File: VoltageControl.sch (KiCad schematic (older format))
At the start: 7 parts

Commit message: Annotation completed
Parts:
- gave numbers to parts that had none: 7
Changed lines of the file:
@@
 $EndDescr
 $Comp
-L LMV358 U?
+L LMV358 U201
 U 2 1 57DB8C8A
 P 3700 4100
-F 0 "U?" H 3650 4300 50  0000 L CNN
+F 0 "U201" H 3650 4300 50  0000 L CNN
 F 1 "LMV358" H 3650 3850 50  0000 L CNN
 F 2 "" H 3700 4100 50  0000 C CNN
@@
 $EndComp
 $Comp
-L R R?
+L R R301
 U 1 1 57DB8C91
 P 2600 5200
-F 0 "R?" V 2680 5200 50  0000 C CNN
+F 0 "R301" V 2680 5200 50  0000 C CNN
 F 1 "R" V 2600 5200 50  0000 C CNN
 F 2 "" V 2530 5200 50  0000 C CNN
@@
 $EndComp
 $Comp
-L GND #PWR?
+L GND #PWR302
 U 1 1 57DB8C98
 P 3600 4400
-F 0 "#PWR?" H 3600 4150 50  0001 C CNN
+F 0 "#PWR302" H 3600 4150 50  0001 C CNN
 F 1 "GND" H 3600 4250 50  0000 C CNN
 F 2 "" H 3600 4400 50  0000 C CNN
@@
 $EndComp
 $Comp
-L POT RV?
+L POT RV301
 U 1 1 57DB8C9E
 P 2600 4450
-F 0 "RV?" H 2600 4370 50  0000 C CNN
+F 0 "RV301" H 2600 4370 50  0000 C CNN
 F 1 "POT" H 2600 4450 50  0000 C CNN
 F 2 "" H 2600 4450 50  0000 C CNN
@@
 $EndComp
 $Comp
-L C C?
+L C C301
 U 1 1 57DB8CA5
 P 3200 3450
-F 0 "C?" H 3225 3550 50  0000 L CNN
+F 0 "C301" H 3225 3550 50  0000 L CNN
 F 1 "C" H 3225 3350 50  0000 L CNN
 F 2 "" H 3238 3300 50  0000 C CNN
@@
 $EndComp
 $Comp
-L GND #PWR?
+L GND #PWR301
 U 1 1 57DB8CAC
 P 3200 3600
-F 0 "#PWR?" H 3200 3350 50  0001 C CNN
+F 0 "#PWR301" H 3200 3350 50  0001 C CNN
 F 1 "GND" H 3200 3450 50  0000 C CNN
 F 2 "" H 3200 3600 50  0000 C CNN
@@
 	1850 2250 2750 2250
 $Comp
-L D D?
+L D D301
 U 1 1 57DB8D2E
 P 4350 4100
-F 0 "D?" H 4350 4200 50  0000 C CNN
+F 0 "D301" H 4350 4200 50  0000 C CNN
 F 1 "D" H 4350 4000 50  0000 C CNN
 F 2 "" H 4350 4100 50  0000 C CNN
@@
 $EndComp
 $Comp
-L R R?
+L R R303
 U 1 1 57DB8DD7
 P 5400 4950
-F 0 "R?" V 5480 4950 50  0000 C CNN
+F 0 "R303" V 5480 4950 50  0000 C CNN
 F 1 "1k" V 5400 4950 50  0000 C CNN
 F 2 "" V 5330 4950 50  0000 C CNN
@@
 $EndComp
 $Comp
-L R R?
+L R R302
 U 1 1 57DB8E45
 P 5400 4400
-F 0 "R?" V 5480 4400 50  0000 C CNN
+F 0 "R302" V 5480 4400 50  0000 C CNN
 F 1 "9k" V 5400 4400 50  0000 C CNN
 F 2 "" V 5330 4400 50  0000 C CNN

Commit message: Add initial layout
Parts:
- C301: footprint (none) -> Capacitors_SMD:C_0805
- D301: footprint (none) -> Diodes_SMD:SMB-SMC_Universal_Handsoldering; MPN (none) -> 1N914BWT
- R301, R302, R303: footprint (none) -> Resistors_SMD:R_0805
- RV301: footprint (none) -> Potentiometers:Potentiometer_WirePads_largePads
- U301: renamed from U201; footprint (none) -> SMD_Packages:SOIC-8-N
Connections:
- net at R301.1, RV301.3: now also U301.3 (+); no longer U301.5 (+)
- net at R302.2, R303.1: now also U301.2 (-); no longer U301.6 (-)
- net at D301.1 (K): now also U301.1; no longer U301.7
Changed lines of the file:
@@
 $EndDescr
 $Comp
-L LMV358 U201
-U 2 1 57DB8C8A
+L LMV358 U301
+U 1 1 57DB8C8A
 P 3700 4100
-F 0 "U201" H 3650 4300 50  0000 L CNN
+F 0 "U301" H 3650 4300 50  0000 L CNN
 F 1 "LMV358" H 3650 3850 50  0000 L CNN
-F 2 "" H 3700 4100 50  0000 C CNN
+F 2 "SMD_Packages:SOIC-8-N" H 3700 4100 50  0001 C CNN
 F 3 "" H 3700 4100 50  0000 C CNN
-	2    3700 4100
+	1    3700 4100
 	1    0    0    -1
 $EndComp
@@
 F 0 "R301" V 2680 5200 50  0000 C CNN
 F 1 "R" V 2600 5200 50  0000 C CNN
-F 2 "" V 2530 5200 50  0000 C CNN
+F 2 "Resistors_SMD:R_0805" V 2530 5200 50  0001 C CNN
 F 3 "" H 2600 5200 50  0000 C CNN
 	1    2600 5200
@@
 $EndComp
 $Comp
-L GND #PWR302
+L GND #PWR05
 U 1 1 57DB8C98
 P 3600 4400
-F 0 "#PWR302" H 3600 4150 50  0001 C CNN
+F 0 "#PWR05" H 3600 4150 50  0001 C CNN
 F 1 "GND" H 3600 4250 50  0000 C CNN
 F 2 "" H 3600 4400 50  0000 C CNN
@@
 F 0 "RV301" H 2600 4370 50  0000 C CNN
 F 1 "POT" H 2600 4450 50  0000 C CNN
-F 2 "" H 2600 4450 50  0000 C CNN
+F 2 "Potentiometers:Potentiometer_WirePads_largePads" H 2600 4450 50  0001 C CNN
 F 3 "" H 2600 4450 50  0000 C CNN
 	1    2600 4450
@@
 F 0 "C301" H 3225 3550 50  0000 L CNN
 F 1 "C" H 3225 3350 50  0000 L CNN
-F 2 "" H 3238 3300 50  0000 C CNN
+F 2 "Capacitors_SMD:C_0805" H 3238 3300 50  0001 C CNN
 F 3 "" H 3200 3450 50  0000 C CNN
 	1    3200 3450
@@
 $EndComp
 $Comp
-L GND #PWR301
+L GND #PWR06
 U 1 1 57DB8CAC
 P 3200 3600
-F 0 "#PWR301" H 3200 3350 50  0001 C CNN
+F 0 "#PWR06" H 3200 3350 50  0001 C CNN
 F 1 "GND" H 3200 3450 50  0000 C CNN
 F 2 "" H 3200 3600 50  0000 C CNN
@@
 F 0 "D301" H 4350 4200 50  0000 C CNN
 F 1 "D" H 4350 4000 50  0000 C CNN
-F 2 "" H 4350 4100 50  0000 C CNN
-F 3 "" H 4350 4100 50  0000 C CNN
+F 2 "Diodes_SMD:SMB-SMC_Universal_Handsoldering" H 4350 4100 50  0001 C CNN
+F 3 "http://www.fairchildsemi.com/datasheets/1N/1N914BWT.pdf" H 4350 4100 50  0001 C CNN
+F 4 "1N914BWT" H 4350 4100 60  0001 C CNN "MPN"
 	1    4350 4100
 	1    0    0    -1
@@
 F 0 "R303" V 5480 4950 50  0000 C CNN
 F 1 "1k" V 5400 4950 50  0000 C CNN
-F 2 "" V 5330 4950 50  0000 C CNN
+F 2 "Resistors_SMD:R_0805" V 5330 4950 50  0001 C CNN
 F 3 "" H 5400 4950 50  0000 C CNN
 	1    5400 4950
@@
 F 0 "R302" V 5480 4400 50  0000 C CNN
 F 1 "9k" V 5400 4400 50  0000 C CNN
-F 2 "" V 5330 4400 50  0000 C CNN
+F 2 "Resistors_SMD:R_0805" V 5330 4400 50  0001 C CNN
 F 3 "" H 5400 4400 50  0000 C CNN
 	1    5400 4400

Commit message: Add heat sink footprint
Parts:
- D301: MPN 1N914BWT -> CD214B-R3600
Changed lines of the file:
@@
 F 1 "D" H 4350 4000 50  0000 C CNN
 F 2 "Diodes_SMD:SMB-SMC_Universal_Handsoldering" H 4350 4100 50  0001 C CNN
-F 3 "http://www.fairchildsemi.com/datasheets/1N/1N914BWT.pdf" H 4350 4100 50  0001 C CNN
-F 4 "1N914BWT" H 4350 4100 60  0001 C CNN "MPN"
+F 3 "http://www.bourns.com/docs/Product-Datasheets/CD214B-R350_R31000.pdf" H 4350 4100 50  0001 C CNN
+F 4 "CD214B-R3600" H 4350 4100 60  0001 C CNN "MPN"
 	1    4350 4100
 	1    0    0    -1

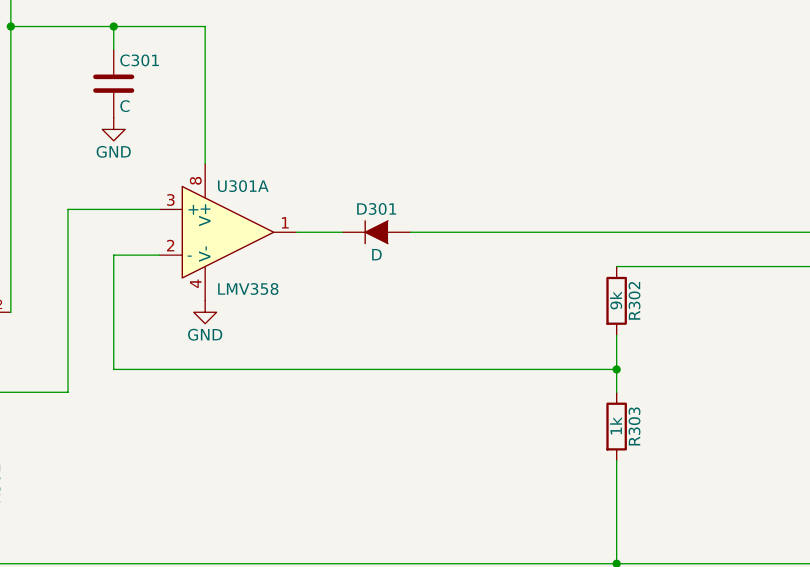
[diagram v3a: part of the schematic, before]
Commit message: Remove extra erroneus LMV358
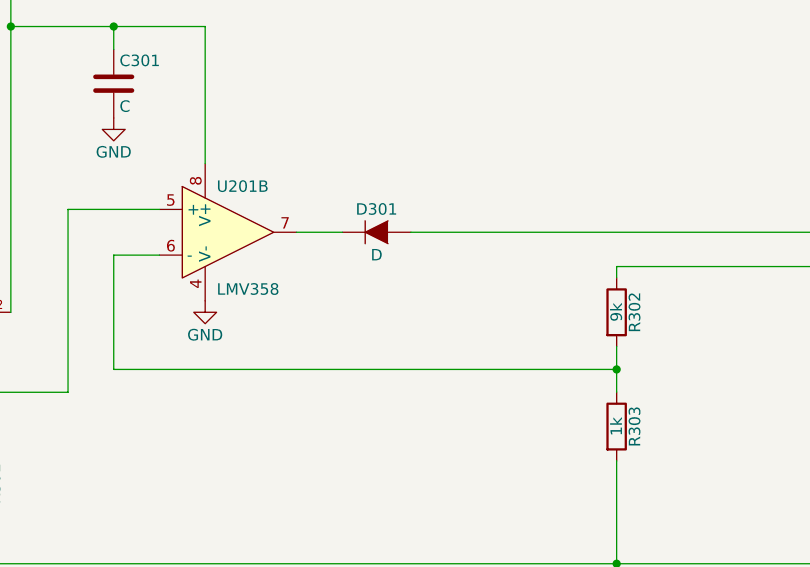
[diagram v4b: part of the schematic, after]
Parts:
- removed U301: LMV358, SMD_Packages:SOIC-8-N, symbol LMV358
- added U201: LMV358, SMD_Packages:SOIC-8-N, symbol LMV358
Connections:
- net 2.7V: now also U201.8 (V+)
- net GND: now also U201.4 (V-)
- net at D301.1 (K): now also U201.7
- net at R302.2, R303.1: now also U201.6 (-)
- net at R301.1, RV301.3: now also U201.5 (+)
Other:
- moved on the sheet: R302
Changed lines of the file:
@@
 $EndDescr
-$Comp
-L LMV358 U301
-U 1 1 57DB8C8A
-P 3700 4100
-F 0 "U301" H 3650 4300 50  0000 L CNN
-F 1 "LMV358" H 3650 3850 50  0000 L CNN
-F 2 "SMD_Packages:SOIC-8-N" H 3700 4100 50  0001 C CNN
-F 3 "" H 3700 4100 50  0000 C CNN
-	1    3700 4100
-	1    0    0    -1
-$EndComp
 $Comp
 L R R301
@@
 L R R302
 U 1 1 57DB8E45
-P 5400 4400
-F 0 "R302" V 5480 4400 50  0000 C CNN
-F 1 "9k" V 5400 4400 50  0000 C CNN
-F 2 "Resistors_SMD:R_0805" V 5330 4400 50  0001 C CNN
-F 3 "" H 5400 4400 50  0000 C CNN
-	1    5400 4400
+P 5400 4450
+F 0 "R302" V 5480 4450 50  0000 C CNN
+F 1 "9k" V 5400 4450 50  0000 C CNN
+F 2 "Resistors_SMD:R_0805" V 5330 4450 50  0001 C CNN
+F 3 "" H 5400 4450 50  0000 C CNN
+	1    5400 4450
 	1    0    0    -1
 $EndComp
@@
 	2600 5350 2600 5550
 Wire Wire Line
-	5400 4550 5400 4800
+	5400 4600 5400 4800
 Connection ~ 5400 4700
 Wire Wire Line
@@
 Text HLabel 6450 4100 2    60   Output ~ 0
 Vcontrol
-Wire Wire Line
-	5400 4250 6450 4250
 Text HLabel 6450 4250 2    60   Output ~ 0
 Current_Sink+
@@
 Text HLabel 6450 5550 2    60   Output ~ 0
 Current_Sink-
+$Comp
+L LMV358 U201
+U 2 1 57E9A810
+P 3700 4100
+F 0 "U201" H 3650 4300 50  0000 L CNN
+F 1 "LMV358" H 3650 3850 50  0000 L CNN
+F 2 "SMD_Packages:SOIC-8-N" H 3700 4100 50  0001 C CNN
+F 3 "http://www.st.com/content/ccc/resource/technical/document/datasheet/b9/d8/3b/8f/a1/8f/46/01/CD00079372.pdf/files/CD00079372.pdf/jcr:content/translations/en.CD00079372.pdf" H 3700 4100 50  0001 C CNN
+F 4 "LMV358IDT" H 3700 4100 60  0001 C CNN "MPN"
+	2    3700 4100
+	1    0    0    -1
+$EndComp
+Wire Wire Line
+	5400 4300 5400 4250
+Wire Wire Line
+	5400 4250 6450 4250
 $EndSCHEMATC

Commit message: Add potentiometers
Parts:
- RV301: footprint Potentiometers:Potentiometer_WirePads_largePads -> current:P090L-02F25BR10K
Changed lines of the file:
@@
 F 0 "RV301" H 2600 4370 50  0000 C CNN
 F 1 "POT" H 2600 4450 50  0000 C CNN
-F 2 "Potentiometers:Potentiometer_WirePads_largePads" H 2600 4450 50  0001 C CNN
+F 2 "current:P090L-02F25BR10K" H 2600 4450 50  0001 C CNN
 F 3 "" H 2600 4450 50  0000 C CNN
 	1    2600 4450

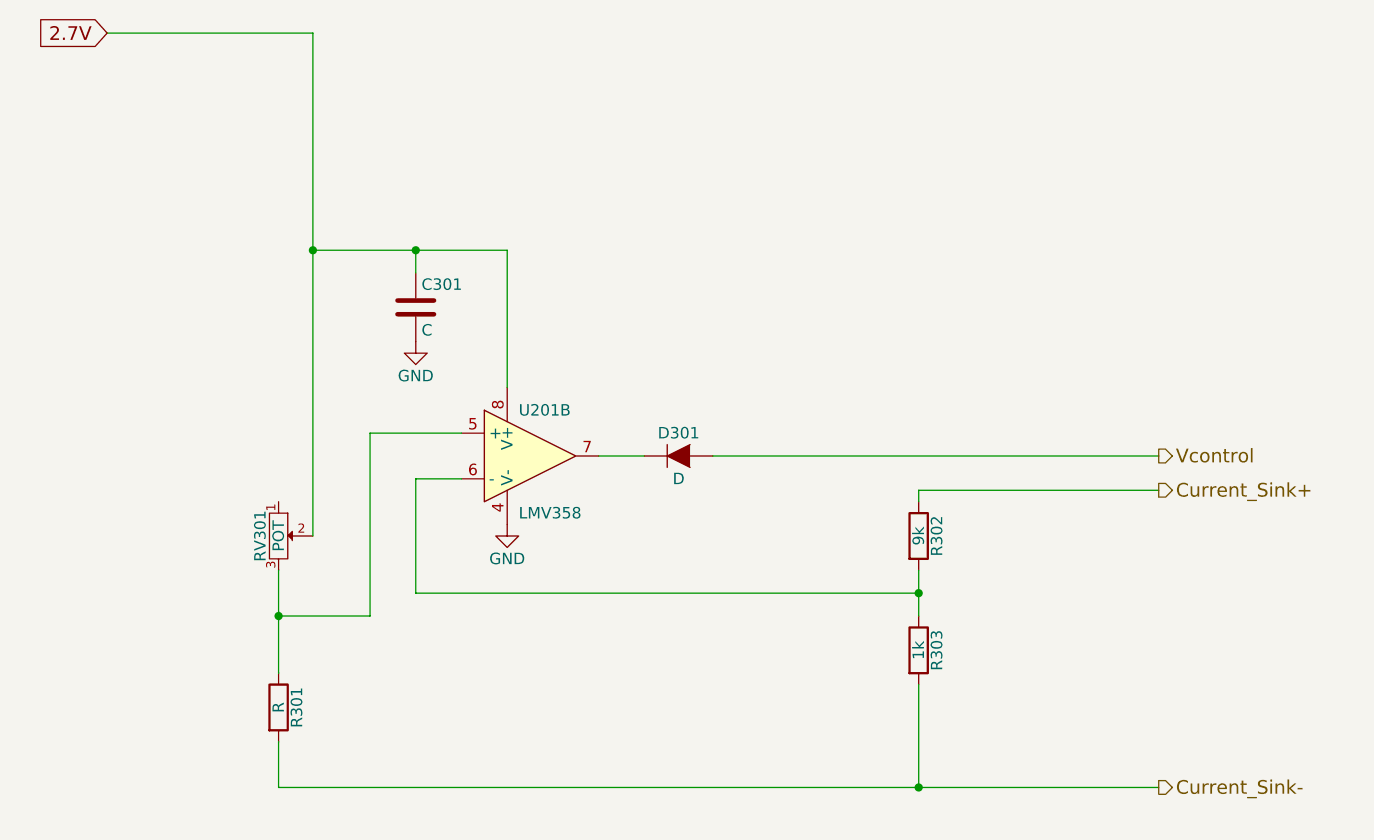
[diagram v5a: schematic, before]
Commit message: Fixed divider resistors and found values
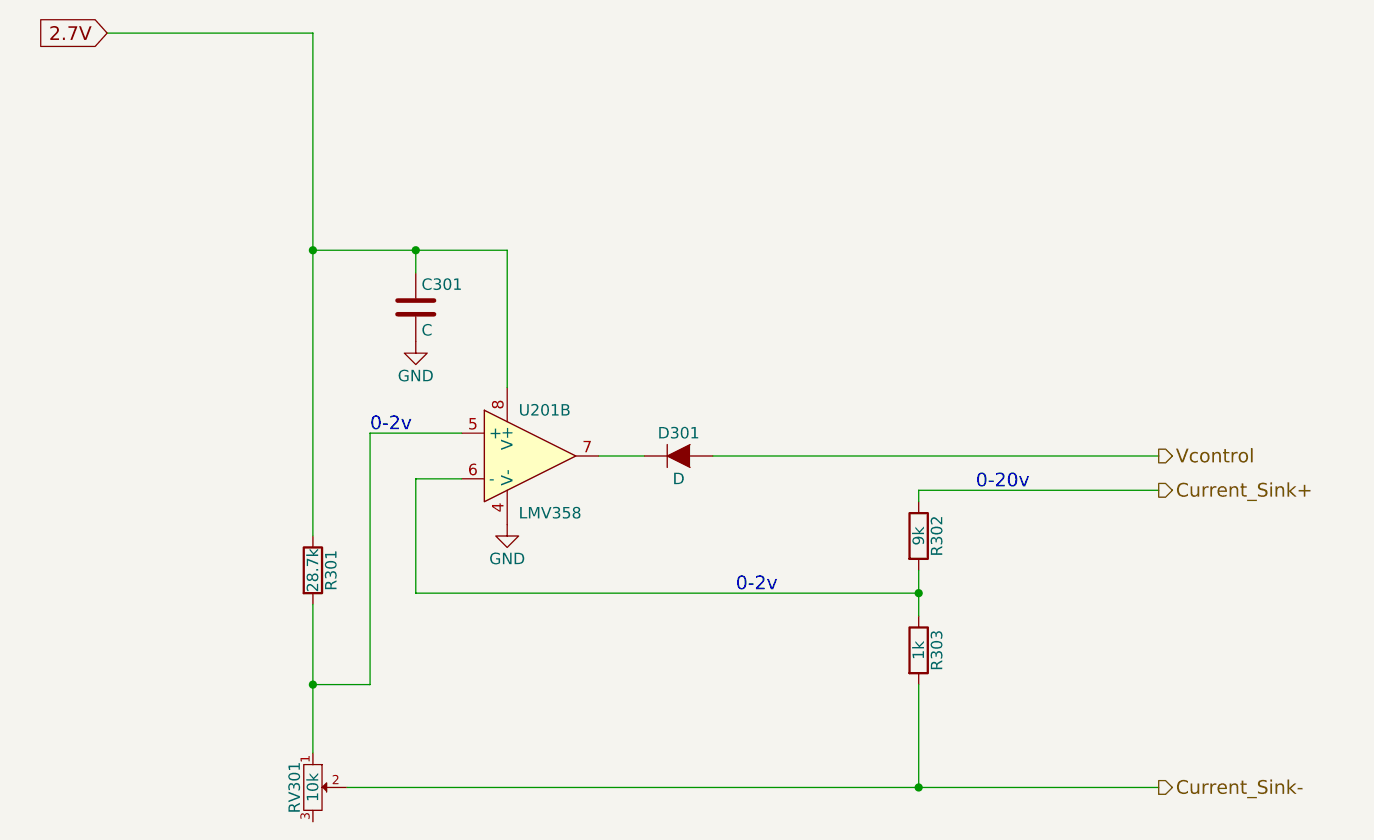
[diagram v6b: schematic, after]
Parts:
- R301: value R -> 28.7k
- RV301: value POT -> 10k
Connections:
- net 2.7V: now also R301.1; no longer RV301.2
- net Current_Sink-: now also RV301.2; no longer R301.2
- net at RV301.1: now also R301.2, U201.5 (+)
- now unconnected: RV301.3
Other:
- note added: "0-20v"
- note added: "0-2v"
- moved on the sheet: R301, RV301
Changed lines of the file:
@@
 L R R301
 U 1 1 57DB8C91
-P 2600 5200
-F 0 "R301" V 2680 5200 50  0000 C CNN
-F 1 "R" V 2600 5200 50  0000 C CNN
-F 2 "Resistors_SMD:R_0805" V 2530 5200 50  0001 C CNN
-F 3 "" H 2600 5200 50  0000 C CNN
-	1    2600 5200
+P 2750 4600
+F 0 "R301" V 2830 4600 50  0000 C CNN
+F 1 "28.7k" V 2750 4600 50  0000 C CNN
+F 2 "Resistors_SMD:R_0805" V 2680 4600 50  0001 C CNN
+F 3 "" H 2750 4600 50  0000 C CNN
+	1    2750 4600
 	1    0    0    -1
 $EndComp
@@
 L POT RV301
 U 1 1 57DB8C9E
-P 2600 4450
-F 0 "RV301" H 2600 4370 50  0000 C CNN
-F 1 "POT" H 2600 4450 50  0000 C CNN
-F 2 "current:P090L-02F25BR10K" H 2600 4450 50  0001 C CNN
-F 3 "" H 2600 4450 50  0000 C CNN
-	1    2600 4450
+P 2750 5550
+F 0 "RV301" H 2750 5470 50  0000 C CNN
+F 1 "10k" H 2750 5550 50  0000 C CNN
+F 2 "current:P090L-02F25BR10K" H 2750 5550 50  0001 C CNN
+F 3 "" H 2750 5550 50  0000 C CNN
+	1    2750 5550
 	0    1    1    0
 $EndComp
@@
 	3200 4700 5400 4700
 Wire Wire Line
-	2600 4600 2600 5050
-Wire Wire Line
 	3400 4000 3000 4000
 Wire Wire Line
-	3000 4000 3000 4800
+	3000 4000 3000 5100
 Wire Wire Line
-	3000 4800 2600 4800
-Connection ~ 2600 4800
-Wire Wire Line
-	2600 5550 6450 5550
+	2900 5550 6450 5550
 Wire Wire Line
 	2750 2250 2750 4450
@@
 $EndComp
 Wire Wire Line
-	2600 5350 2600 5550
-Wire Wire Line
 	5400 4600 5400 4800
 Connection ~ 5400 4700
@@
 Wire Wire Line
 	5400 4250 6450 4250
+Wire Wire Line
+	2750 5400 2750 4750
+Wire Wire Line
+	3000 5100 2750 5100
+Connection ~ 2750 5100
+Text Notes 4600 4700 0    60   ~ 0
+0-2v
+Text Notes 3000 4000 0    60   ~ 0
+0-2v
+Text Notes 5650 4250 0    60   ~ 0
+0-20v
 $EndSCHEMATC

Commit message: Version 3 of the layout
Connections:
- net at R301.2, RV301.1: now also U201.3 (+); no longer U201.5 (+)
- net at D301.1 (K): now also U201.1; no longer U201.7
- net at R302.2, R303.1: now also U201.2 (-); no longer U201.6 (-)
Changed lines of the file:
@@
 $EndComp
 $Comp
-L GND #PWR05
+L GND #PWR04
 U 1 1 57DB8C98
 P 3600 4400
-F 0 "#PWR05" H 3600 4150 50  0001 C CNN
+F 0 "#PWR04" H 3600 4150 50  0001 C CNN
 F 1 "GND" H 3600 4250 50  0000 C CNN
 F 2 "" H 3600 4400 50  0000 C CNN
@@
 $EndComp
 $Comp
-L GND #PWR06
+L GND #PWR05
 U 1 1 57DB8CAC
 P 3200 3600
-F 0 "#PWR06" H 3200 3350 50  0001 C CNN
+F 0 "#PWR05" H 3200 3350 50  0001 C CNN
 F 1 "GND" H 3200 3450 50  0000 C CNN
 F 2 "" H 3200 3600 50  0000 C CNN
@@
 $Comp
 L LMV358 U201
-U 2 1 57E9A810
+U 1 1 57E9A810
 P 3700 4100
 F 0 "U201" H 3650 4300 50  0000 L CNN
@@
 F 3 "http://www.st.com/content/ccc/resource/technical/document/datasheet/b9/d8/3b/8f/a1/8f/46/01/CD00079372.pdf/files/CD00079372.pdf/jcr:content/translations/en.CD00079372.pdf" H 3700 4100 50  0001 C CNN
 F 4 "LMV358IDT" H 3700 4100 60  0001 C CNN "MPN"
-	2    3700 4100
+	1    3700 4100
 	1    0    0    -1
 $EndComp
